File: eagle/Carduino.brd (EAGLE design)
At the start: 88 x 88 mm, 88 parts, among them IC11 RV-3028-C7_32.768KHZ_1PPM_TA_Q, IC2 FT232RL, IC3 SN74HCS596DR, IC4 SN74HCS596DR, IC5 SN74HCS596DR, IC6 SN74HCS596DR, IC7 NTMD4184PFR2G, IC8 ATTINY404-SSNR, IC9 MCP73831T-3ACI_OT, U1 BAT-HLD-012-SMT

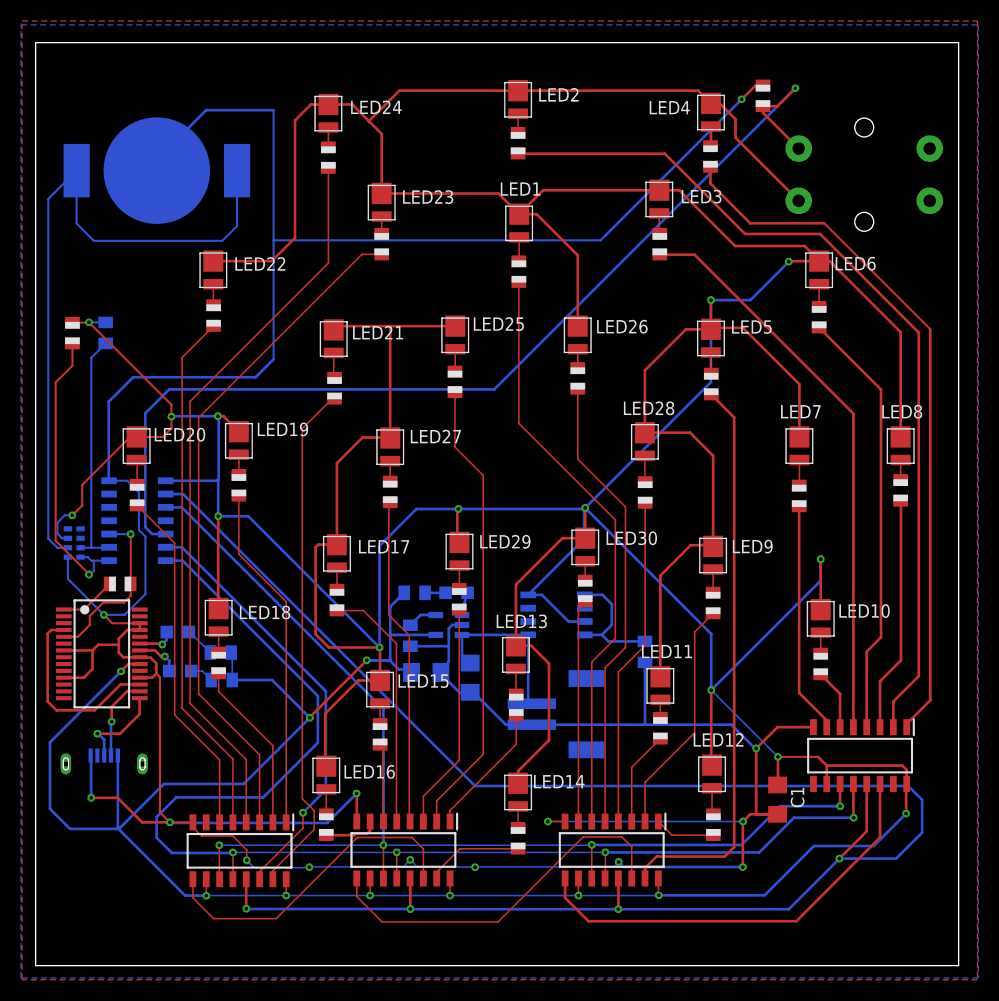
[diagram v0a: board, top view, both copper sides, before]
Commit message: swaping ftdi chip with CP2102N
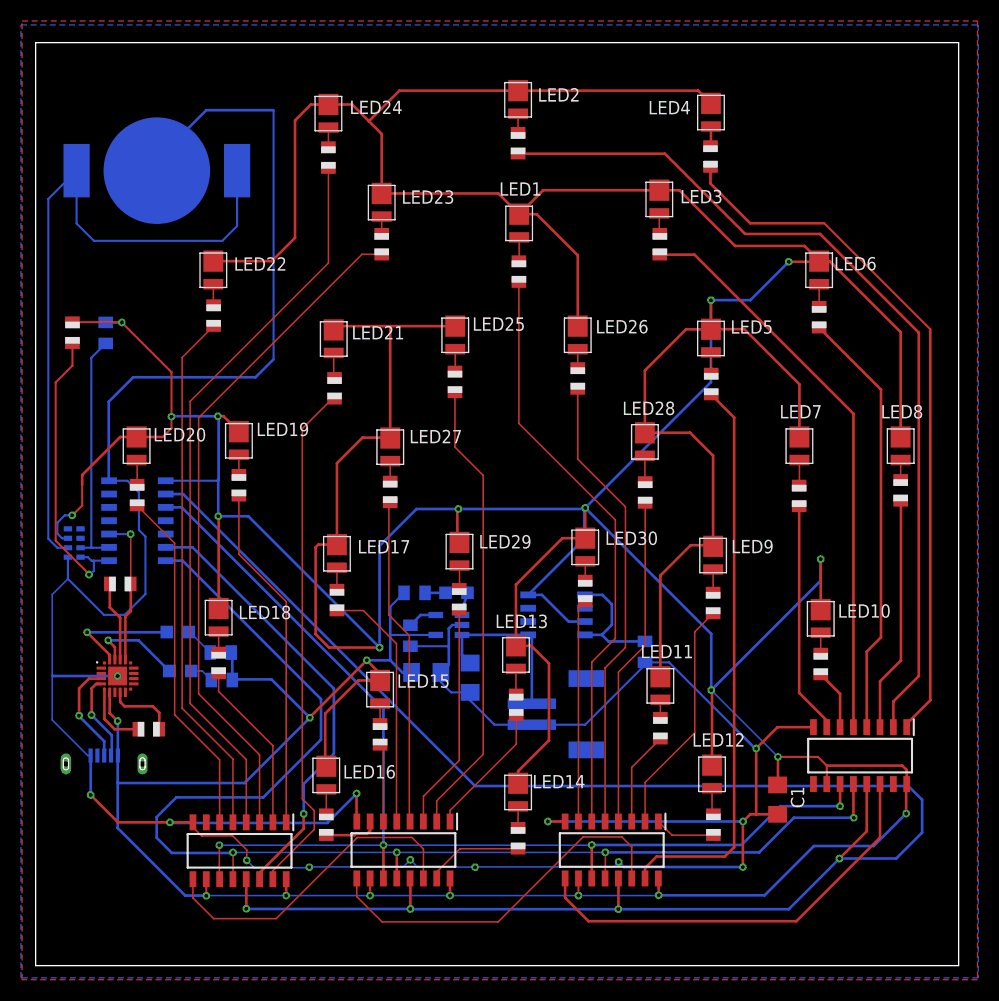
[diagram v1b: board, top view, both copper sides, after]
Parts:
- removed IC2: FT232RL, ftdichip:SSOP28
- removed R6: 4.7K, adafruit:R0805
- removed S1: (no value), adafruit:B3F-40XX-ROUND
- added IC1: CP2102N-A02-GQFN20, SamacSys_Parts:CP2102NA02GQFN20
- added R23: 1K, adafruit:R0805
- CN1: value (none) -> Battery
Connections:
- net N$35 renamed OE
- net N$96 renamed SRCLK
- net N$97 renamed RCLK
- net N$98 renamed SER
- removed net N$101: IC2.17, IC2.4
- removed net N$102: IC2.1, R1.1
- removed net N$106: IC2.23, TX.C
- removed net N$107: IC2.22, RX.C
- removed net N$34: IC8.5, R6.1, S1.2
- new net N$41: IC1.20, TX.C
- new net N$42: IC1.19, RX.C
- new net N$43: IC1.18, R1.1
- new net N$44: IC1.6, R23.1
- new net N$45: IC1.9, R23.2
- net GND: now also IC1.21; no longer IC2.11, IC2.18, IC2.21, IC2.25, IC2.26, IC2.7, R6.2
- net N$100: now also IC1.4; no longer IC2.15
- net N$103: now also IC1.17; no longer IC2.5
- net N$99: now also IC1.5; no longer IC2.16
- net VCC: now also IC1.7; no longer IC2.20, S1.4
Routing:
- net N$34: track 97.1 -> 0.00 mm, vias 1 -> 0
- net GND: track 364.9 -> 295.5 mm, vias 14 -> 13
- net VCC: track 768.4 -> 733.7 mm
- net N$101: track 18.3 -> 0.00 mm
- net N$41: track 0.00 -> 11.1 mm, vias 0 -> 1
- net N$42: track 0.00 -> 9.14 mm, vias 0 -> 1
- net N$43: track 0.00 -> 7.64 mm
- net N$45: track 0.00 -> 6.65 mm
- net N$44: track 0.00 -> 6.48 mm
- net N$102: track 5.39 -> 0.00 mm
- net N$107: track 4.18 -> 0.00 mm, vias 1 -> 0
- net N$106: track 3.57 -> 0.00 mm, vias 1 -> 0
- net N$103: track 16.5 -> 14.3 mm
- net SER: track 41.5 -> 42.7 mm
- net N$100: track 8.74 -> 9.90 mm
